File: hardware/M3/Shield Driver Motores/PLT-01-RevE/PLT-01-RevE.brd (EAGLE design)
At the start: 68.6 x 53.6 mm, 21 parts, among them IC1 L293D, IC2 L293D, X1 22-23-2021, X2 22-23-2021, X3 22-23-2021, X4 22-23-2021, X5 22-23-2021

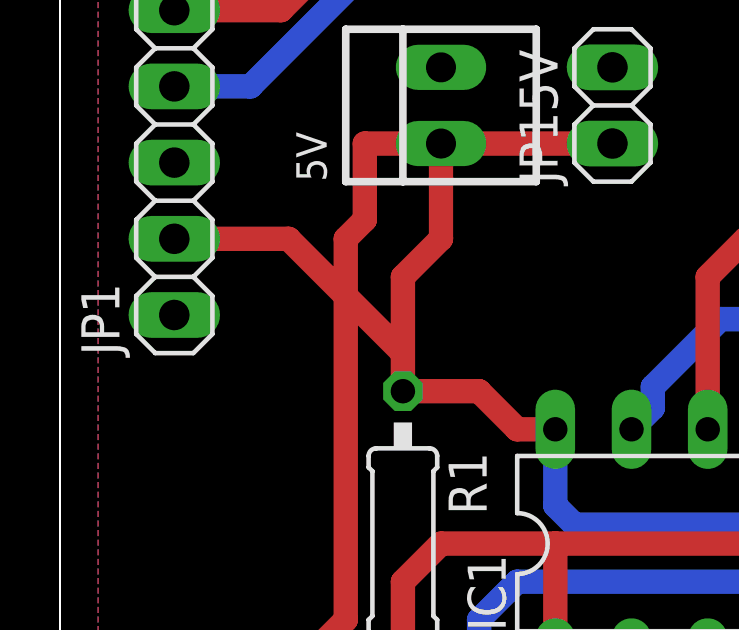
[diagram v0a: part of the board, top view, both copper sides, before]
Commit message: PLT-01-RevE
se modifica Bus de alimentacion en bt para que el conector no este en la misma linea que los demas
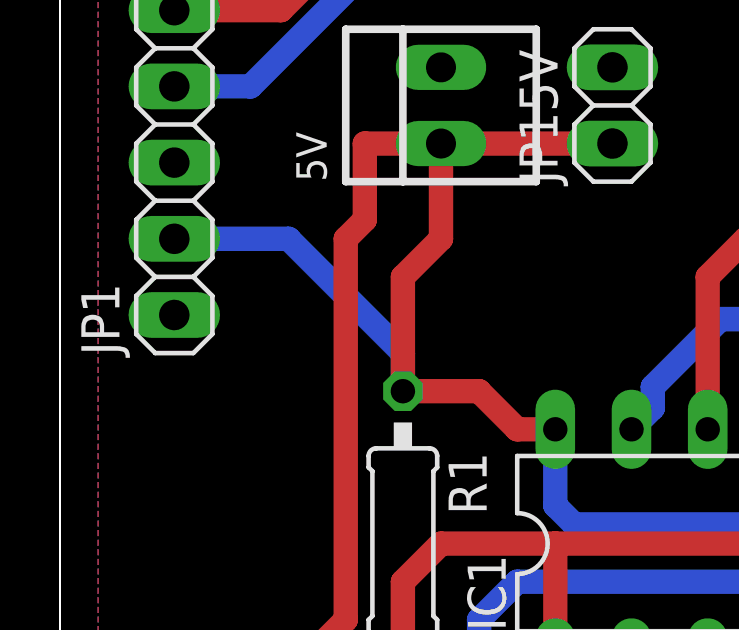
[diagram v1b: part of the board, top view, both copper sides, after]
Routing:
- net 5V: track 143.5 -> 144.7 mm
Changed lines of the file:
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@@
 <wire x1="25.4" y1="33.02" x2="25.4" y2="35.56" width="0.8128" layer="16"/>
 <contactref element="JP1" pad="2"/>
-<wire x1="12.7" y1="41.91" x2="16.51" y2="41.91" width="0.8128" layer="1"/>
-<wire x1="16.51" y1="41.91" x2="20.32" y2="38.1" width="0.8128" layer="1"/>
 <wire x1="20.32" y1="38.1" x2="20.32" y2="36.83" width="0.254" layer="1"/>
+<wire x1="12.7" y1="41.91" x2="16.51" y2="41.91" width="0.8128" layer="16"/>
+<wire x1="16.51" y1="41.91" x2="20.32" y2="38.1" width="0.8128" layer="16"/>
+<wire x1="20.32" y1="38.1" x2="20.32" y2="36.83" width="0.8128" layer="16"/>
 </signal>
 <signal name="N$1">

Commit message: Se agrega bluettoth a placa M3 control de motores. RevE
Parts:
- JP1: device pinhead:1X06 -> pinhead:1X07
- moved JP1 19.8 mm to (14.6, 26.0), turned to 270 degrees
- moved X2 11.4 mm to (24.1, 14.0), turned to 0 degrees
- moved JP212V 5.08 mm to (24.1, 19.1), turned to 0 degrees
- moved JP15V 2.29 mm to (25.4, 47.6)
- moved 5V 1.80 mm to (20.3, 47.6)
- moved R1 1.27 mm to (20.3, 30.5)
- moved JPM1 1.27 mm to (34.3, 48.3)
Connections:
- removed net N$11 (its old number): IC1.10, U$1.D11
- removed net N$19: JP1.5, U$1.D13
- removed net N$22: IC1.15, U$1.D10
- new net 3A1: IC1.10, U$1.D10
- new net 4A1: IC1.15, U$1.D11
- new net GND4: IC2.12
- new net RXBT: JP1.2, U$1.D13
- new net TXBT: JP1.3, U$1.D12
- net 5V: now also JP1.5; no longer JP1.2
- net GND: now also JP1.4; no longer IC2.12, JP1.3
- net N$13: now also JP1.6, JP1.7; no longer JP1.4, U$1.D12
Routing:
- net RXBT: track 0.00 -> 51.2 mm
- net TXBT: track 0.00 -> 44.2 mm
- net 4A1: track 0.00 -> 32.0 mm
- net N$22: track 29.5 -> 0.00 mm
- net N$13: track 31.7 -> 2.54 mm
- net N$19: track 28.0 -> 0.00 mm
- net 3A1: track 0.00 -> 21.0 mm
- net N$11 (its old number): track 20.0 -> 0.00 mm
- net VCC2: track 111.9 -> 105.1 mm
- net 5V: track 144.7 -> 141.4 mm
- net N$11: track 34.1 -> 35.3 mm
- net N$8: track 13.2 -> 14.5 mm
- net N$7: track 13.2 -> 14.5 mm
- net GND: vias 0 -> 1
